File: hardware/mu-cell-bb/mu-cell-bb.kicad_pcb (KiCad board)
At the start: 4 copper layers, 65 x 30 mm, 76 parts, among them IC1 SX1255IWLTRT, J1 TX, J2 RX, J3 EXT_CLK, J4 RPi GPIO, J5 IO, Q1 BC817-40W, Q2 BC817-40W, U1 24LC256, U2 LDK130M33R, Y1 32MHz

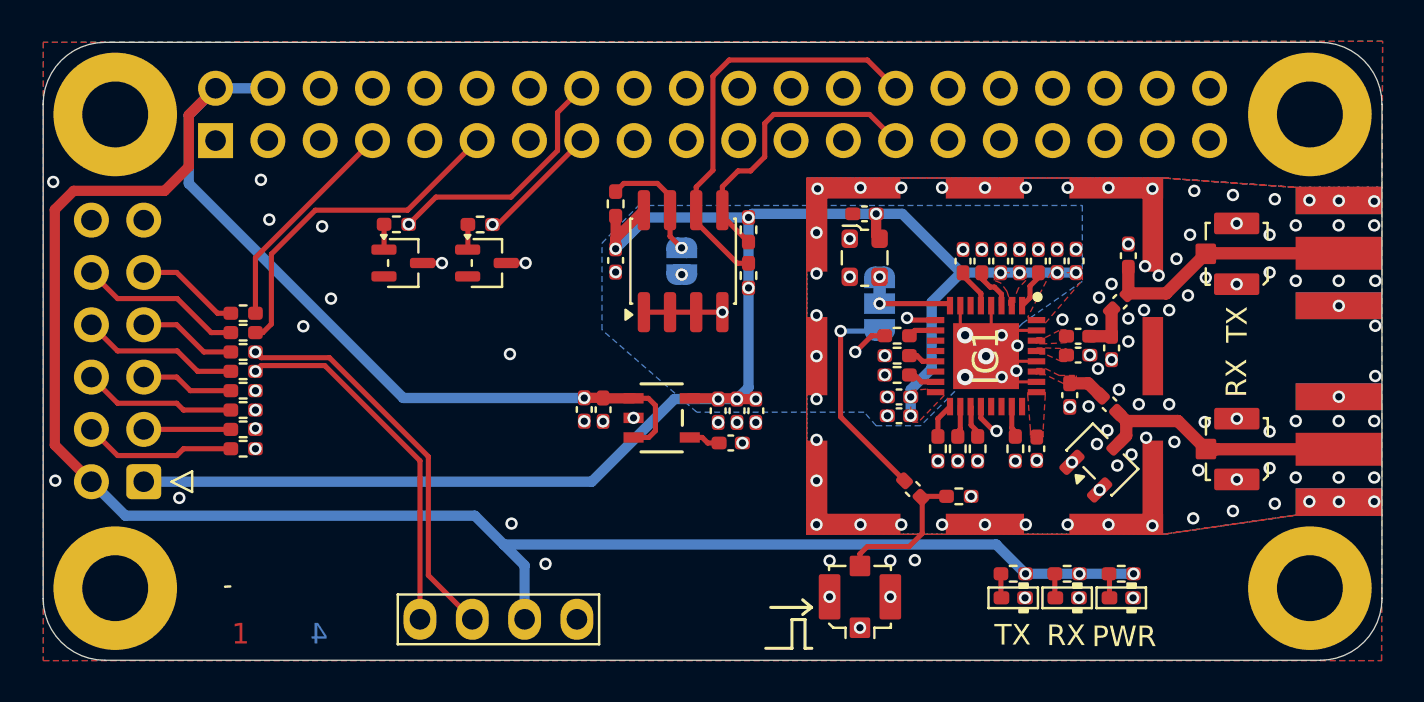
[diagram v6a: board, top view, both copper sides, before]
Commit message: linted readme, moved stuff on PCB
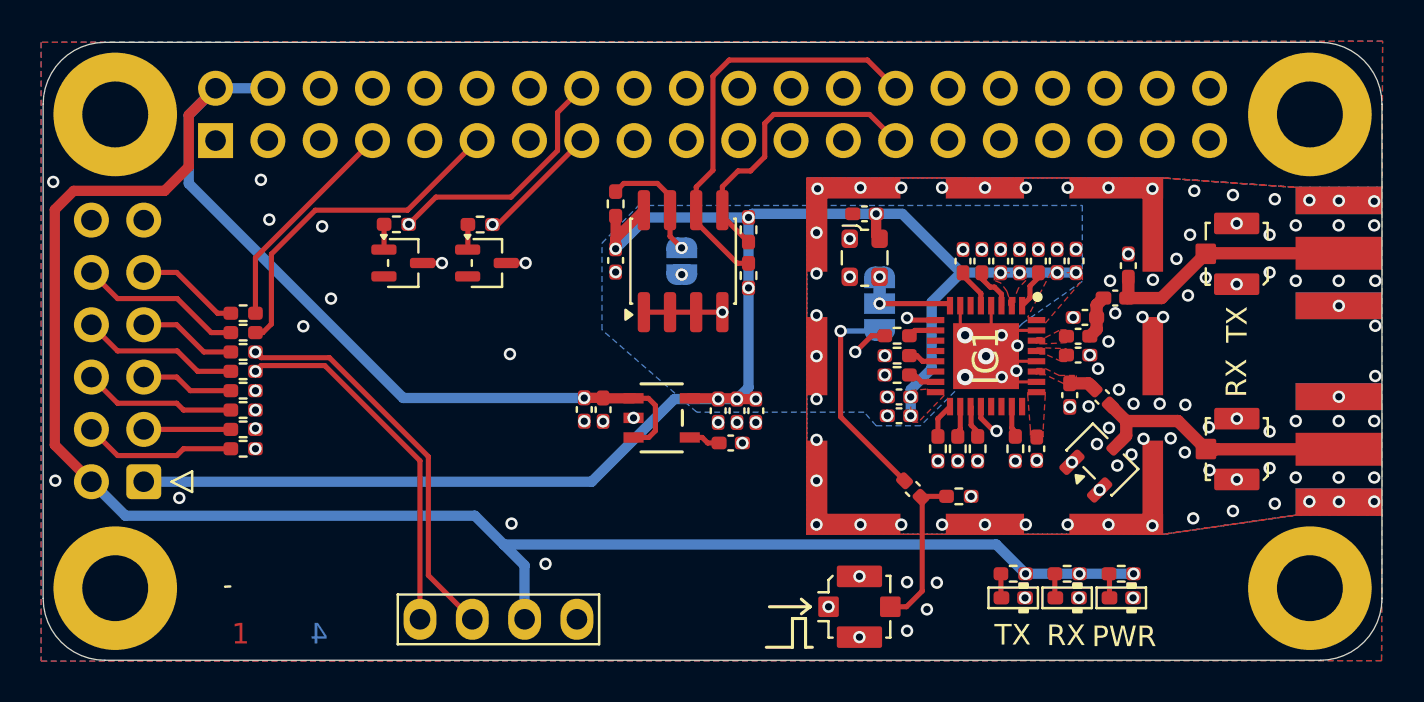
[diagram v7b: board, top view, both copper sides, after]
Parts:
- added LOGO1: ~, OSHW:OSHW-Certification-Mark-Stacked_8x7mm_SilkMask, B.Cu at (177.1, 99.6)
- moved C2 1.97 mm to (171.2, 97.9), turned to 180 degrees
- moved L2 0.50 mm to (172.0, 101.8)
- moved C3 0.48 mm to (173.3, 95.4)
- moved J3 0.48 mm to (160.2, 112.0), turned to 90 degrees
- moved L1 0.29 mm to (172.6, 97.0), turned to 0 degrees
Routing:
- net Net-(J3-In): track 6.91 -> 7.56 mm
- net Net-(LED3-K): track 44.7 -> 44.1 mm
- net /RFI: track 1.83 -> 1.28 mm
- net /RF_RX: track 12.7 -> 13.2 mm
- net GND: vias 142 -> 141
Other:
- board text added: "CLK"
- board text added: "EXT"
- board text added: "INT"
- board text added: "WP"

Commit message: saved changes on PCB
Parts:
- removed LOGO1: ~, OSHW:OSHW-Certification-Mark-Stacked_8x7mm_SilkMask
- added BE000000: ~, OSHW:OSHW-Certification-Mark-Stacked_8x7mm_SilkMask, B.Cu at (135.6, 99.6)
